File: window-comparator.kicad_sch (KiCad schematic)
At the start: 12 parts, among them U1001 TLV9352

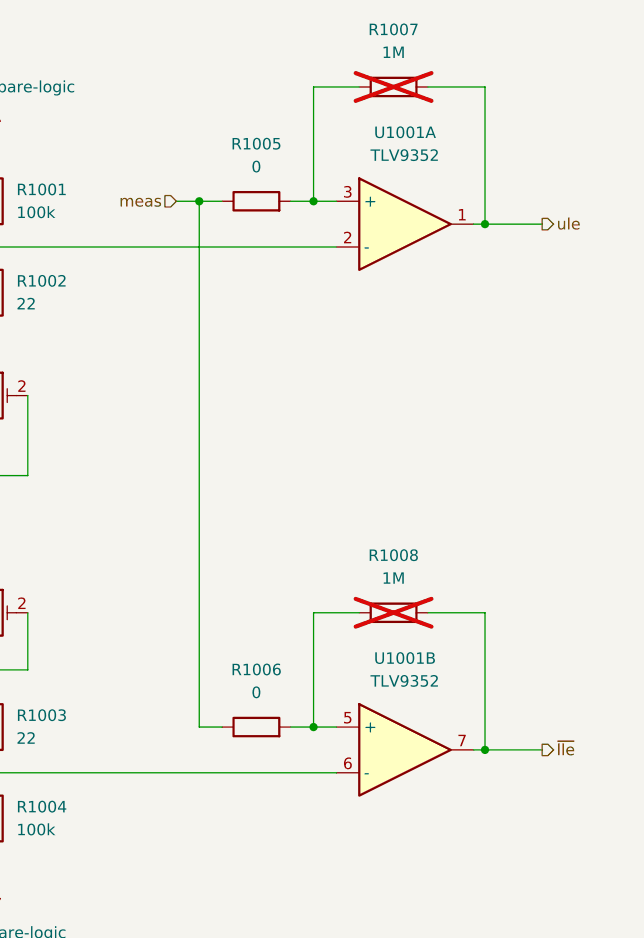
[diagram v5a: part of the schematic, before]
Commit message: add pcb layout for compare-logic sub circuit - prototype
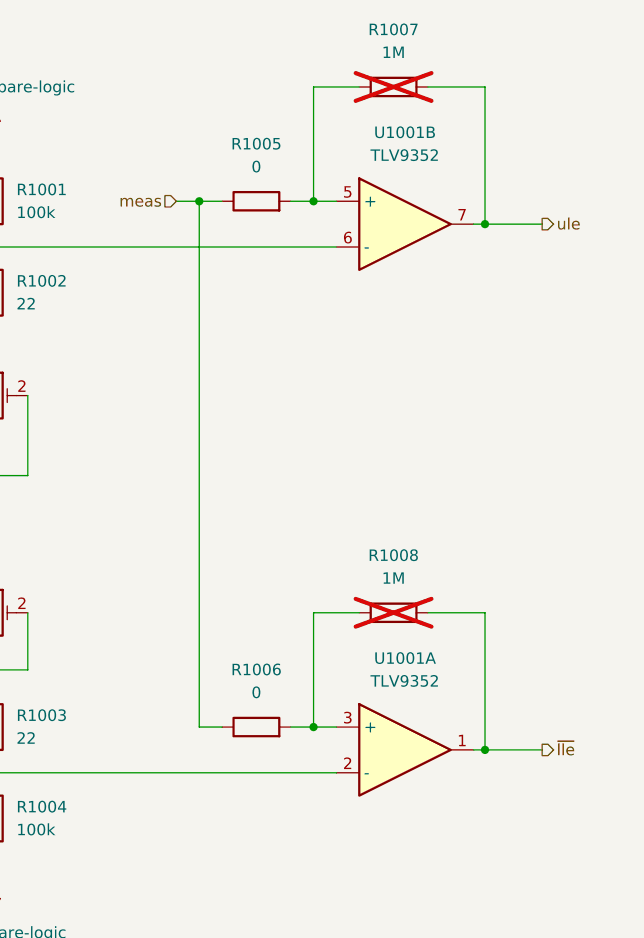
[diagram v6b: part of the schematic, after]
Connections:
- net ule: now also U1001.7; no longer U1001.1
- net ~{lle}: now also U1001.1; no longer U1001.7
- net at R1003.2, R1004.1: now also U1001.2 (-); no longer U1001.6 (-)
- net at R1005.2, R1007.1: now also U1001.5 (+); no longer U1001.3 (+)
- net at R1001.2, R1002.1: now also U1001.6 (-); no longer U1001.2 (-)
- net at R1006.2, R1008.1: now also U1001.3 (+); no longer U1001.5 (+)
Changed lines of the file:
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@@
 		(lib_id "pss:Opamp_Dual")
 		(at 162.56 66.04 0)
-		(unit 1)
+		(unit 2)
 		(exclude_from_sim no)
 		(in_bom yes)
@@
 				(path "/3c438cf7-9350-4e9f-8115-1deba8984176/6d7b7ab4-65f8-454e-98e1-8374f6b5e166/854e83c3-d665-4da7-a2c9-4ae5fb1019c9/e65c3b78-3b2b-4f8a-bb92-3808512b49dd"
 					(reference "U1001")
-					(unit 1)
+					(unit 2)
 				)
 				(path "/3c438cf7-9350-4e9f-8115-1deba8984176/6d7b7ab4-65f8-454e-98e1-8374f6b5e166/854e83c3-d665-4da7-a2c9-4ae5fb1019c9/ff334853-ab60-485c-bb6b-fcb0e80d61f1"
@@
 		(lib_id "pss:Opamp_Dual")
 		(at 162.56 124.46 0)
-		(unit 2)
+		(unit 1)
 		(exclude_from_sim no)
 		(in_bom yes)
@@
 				(path "/3c438cf7-9350-4e9f-8115-1deba8984176/6d7b7ab4-65f8-454e-98e1-8374f6b5e166/854e83c3-d665-4da7-a2c9-4ae5fb1019c9/e65c3b78-3b2b-4f8a-bb92-3808512b49dd"
 					(reference "U1001")
-					(unit 2)
+					(unit 1)
 				)
 				(path "/3c438cf7-9350-4e9f-8115-1deba8984176/6d7b7ab4-65f8-454e-98e1-8374f6b5e166/854e83c3-d665-4da7-a2c9-4ae5fb1019c9/ff334853-ab60-485c-bb6b-fcb0e80d61f1"
